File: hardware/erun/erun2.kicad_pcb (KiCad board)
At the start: 2 copper layers, 73.7 x 92.1 mm, 21 parts, among them J1 Conn_Coaxial, J10 Conn_01x03_Female, J2 HEIDENHAIN_MT25_TTL, J3 TRIGGER_TTL, J4 Conn_01x02_Female, J5 Conn_01x02_Female, J6 Conn_01x02_Female, J7 Conn_01x02_Female, J8 Conn_01x02_Female, J9 Conn_01x03_Female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

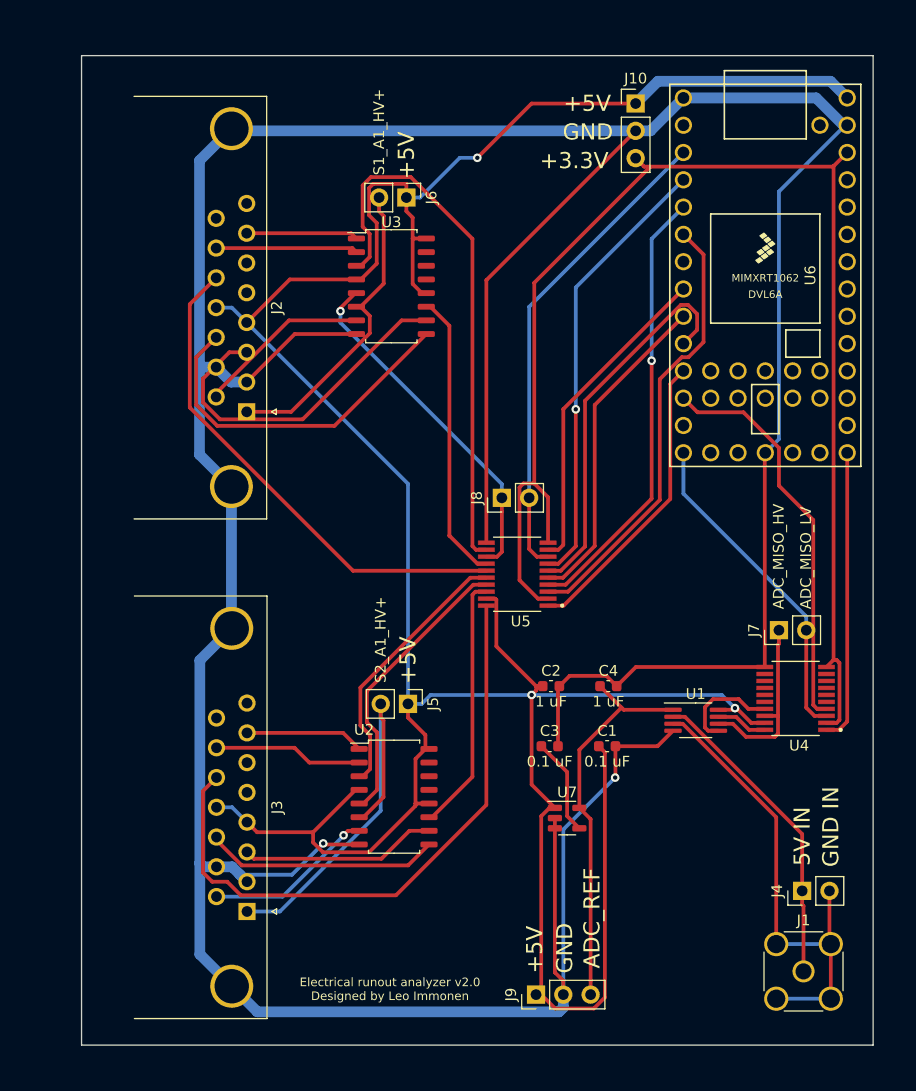
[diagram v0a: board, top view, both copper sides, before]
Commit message: Fixed clearance issues
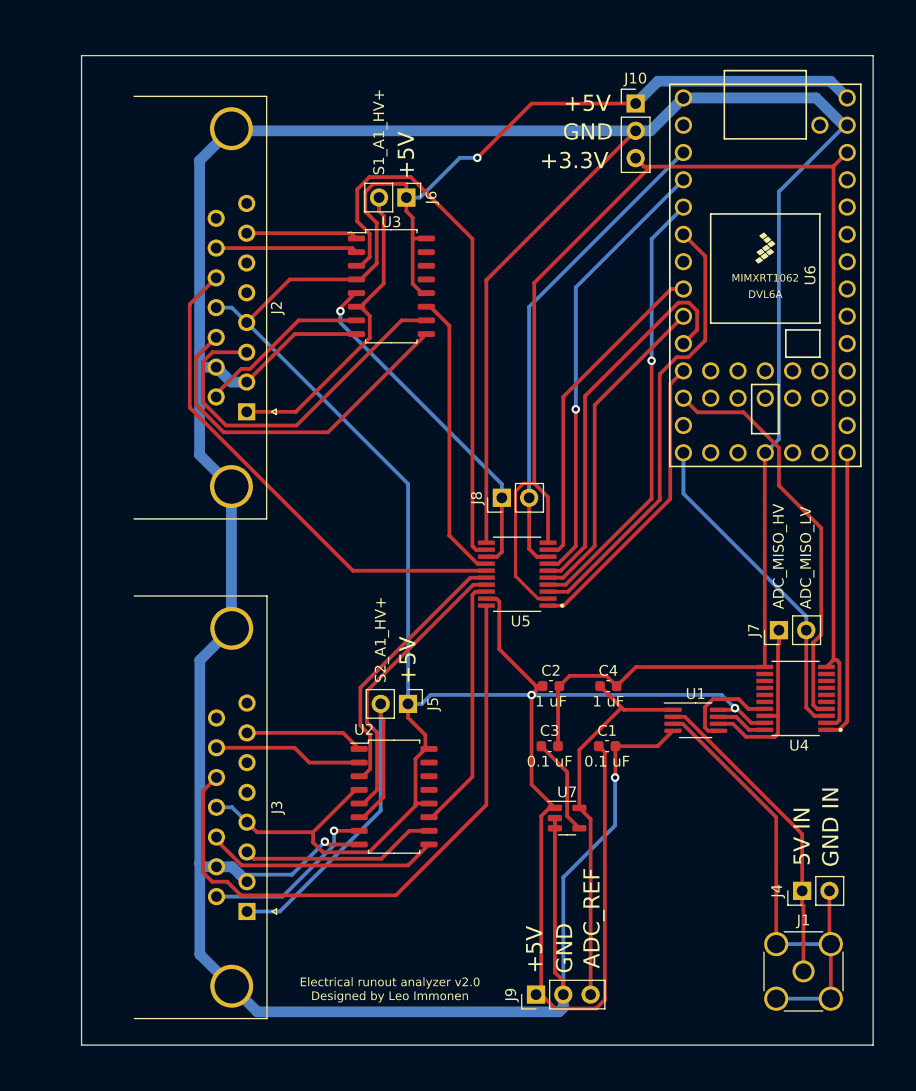
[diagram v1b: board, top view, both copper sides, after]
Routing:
- net /S1_A2_HV+: track 32.5 -> 33.9 mm
- net /S2_A1_HV-: track 15.8 -> 16.6 mm
- net /S1_A0_LV: track 30.1 -> 30.7 mm
- net /ADC_CS_LV: track 37.4 -> 38.1 mm
- net /S1_AS_LV: track 35.7 -> 36.3 mm

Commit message: Fixed some more clearance issues
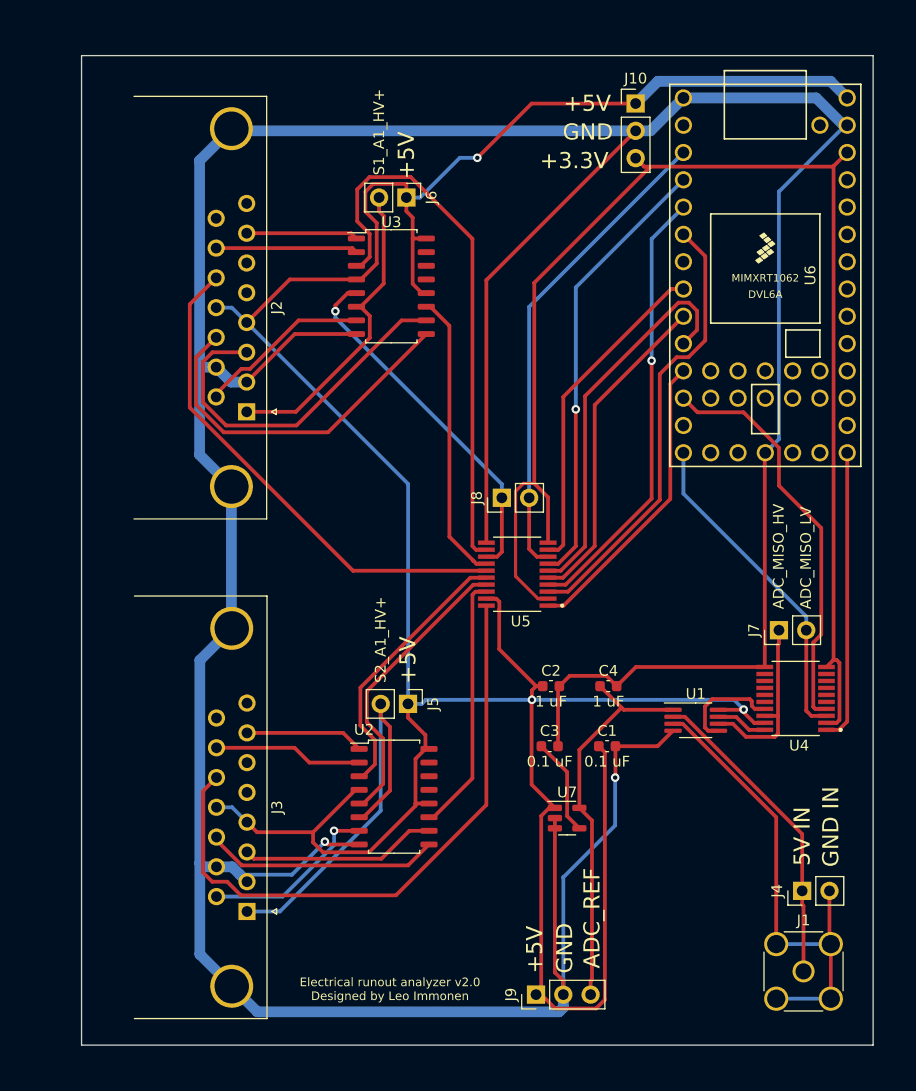
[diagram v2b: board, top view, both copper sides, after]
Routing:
- net /S1_A1_HV: track 32.6 -> 33.4 mm
- net +5V: track 279.1 -> 279.8 mm

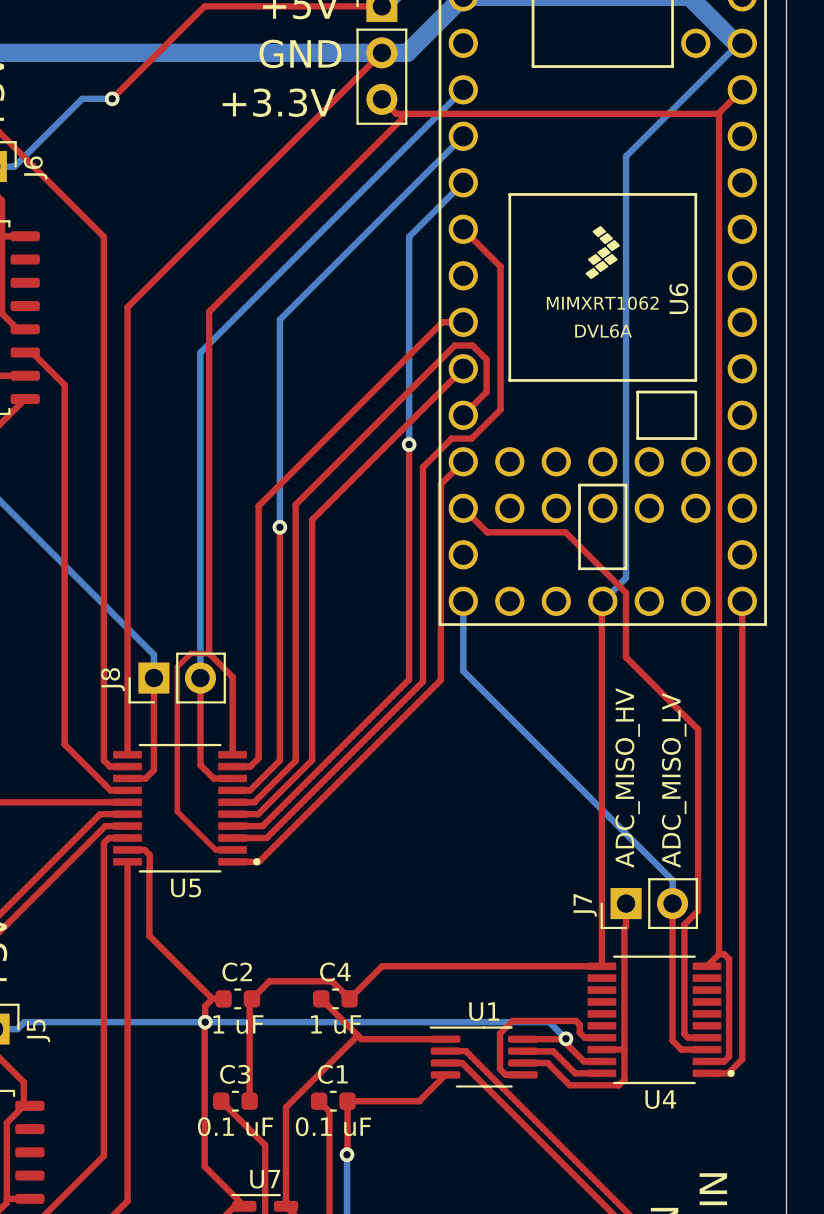
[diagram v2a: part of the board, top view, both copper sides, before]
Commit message: Added capacitors to the board
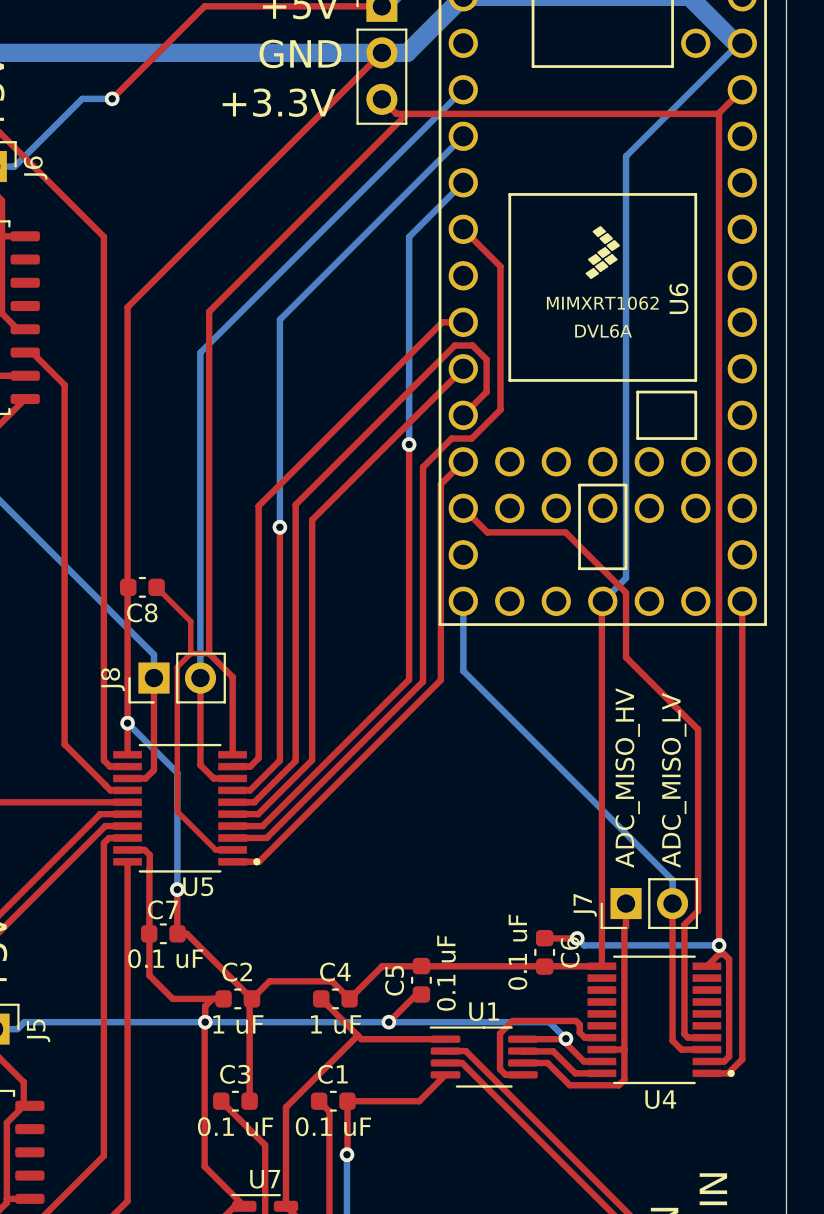
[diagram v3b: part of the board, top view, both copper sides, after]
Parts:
- added C5: 0.1 uF, Capacitor_SMD:C_0603_1608Metric, F.Cu at (63.8, 67.7)
- added C6: 0.1 uF, Capacitor_SMD:C_0603_1608Metric, F.Cu at (70.5, 66.2)
- added C7: 0.1 uF, Capacitor_SMD:C_0603_1608Metric, F.Cu at (49.7, 65.2)
- added C8: 0.1 uF, Capacitor_SMD:C_0603_1608Metric, F.Cu at (48.5, 46.2)
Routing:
- net GND: track 384.0 -> 402.2 mm, vias 2 -> 4
- net +3V3: track 128.6 -> 142.7 mm, vias 0 -> 2
- net +5V: track 279.8 -> 284.0 mm, vias 3 -> 4

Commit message: Added filled zones
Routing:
- added copper zone on B.Cu, net GND
- added copper zone on F.Cu, net GND
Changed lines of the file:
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@@
   (segment (start 74.676 97.79) (end 79.756 97.79) (width 0.35) (layer "B.Cu") (net 85))
   (segment (start 74.676 92.71) (end 79.756 92.71) (width 0.35) (layer "B.Cu") (net 85))
+  (zone (net 1) (net_name "GND") (layers F&B.Cu) (name "GND FILL") (hatch edge 0.508)
+    (connect_pads (clearance 0.508))
+    (min_thickness 0.254) (filled_areas_thickness no)
+    (fill yes (thermal_gap 0.508) (thermal_bridge_width 0.508))
+    (polygon
+      (pts
+        (xy 85.471 6.985)
+        (xy 85.725 104.394)
+        (xy 4.445 104.394)
+        (xy 4.445 6.858)
+      )
+    )
+  )
 )

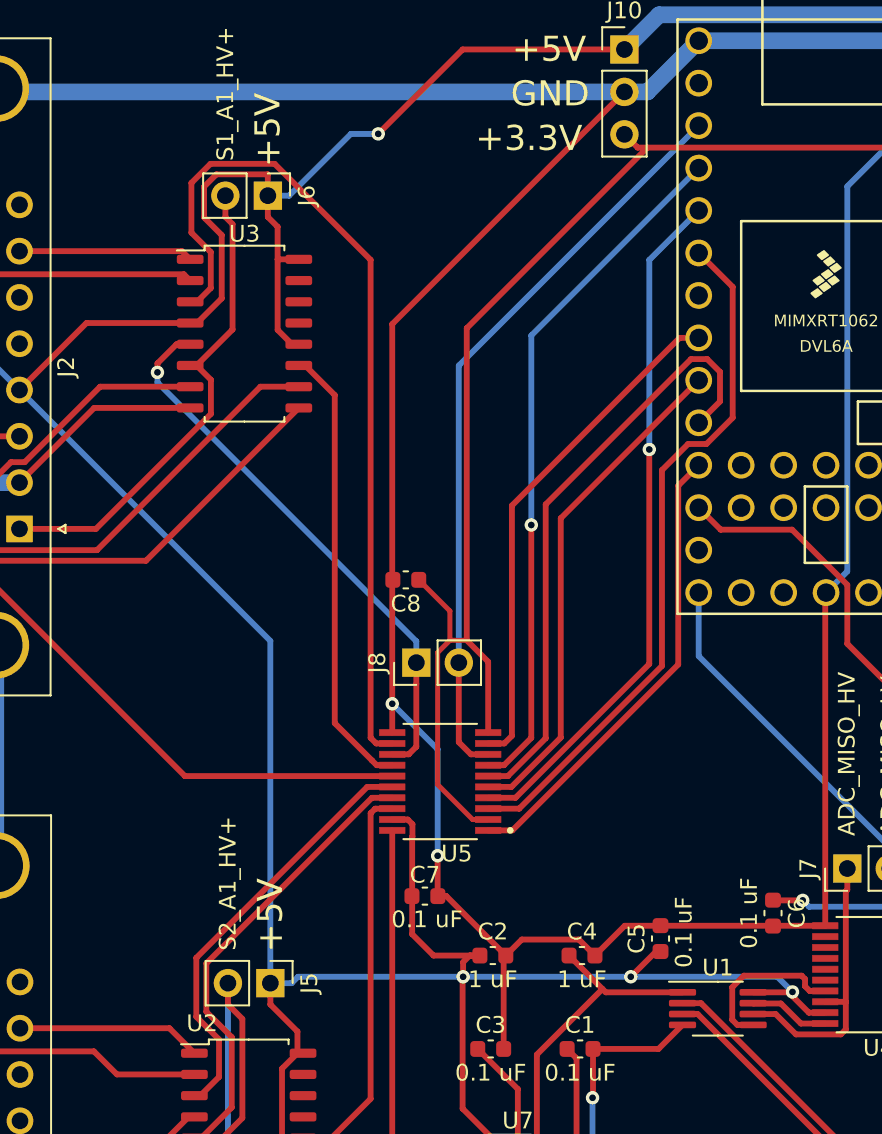
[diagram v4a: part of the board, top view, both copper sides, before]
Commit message: Added vias to filled zones
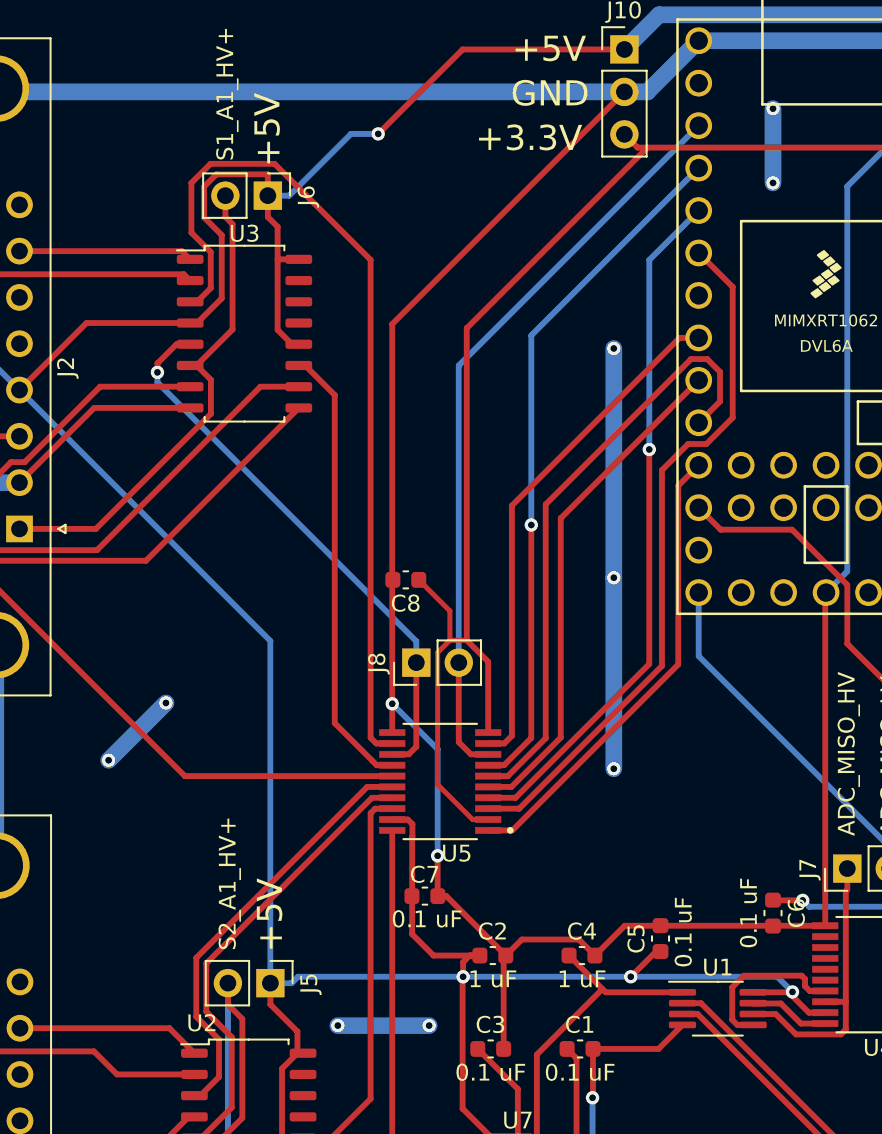
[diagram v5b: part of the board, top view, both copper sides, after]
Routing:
- net GND: track 402.2 -> 442.1 mm, vias 4 -> 13
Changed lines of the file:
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@@
   (segment (start 54.369 68.834) (end 54.496 68.707) (width 0.35) (layer "F.Cu") (net 1))
   (via (at 47.7025 53.6435) (size 0.8) (drill 0.4) (layers "F.Cu" "B.Cu") (net 1))
+  (via (at 30.734 57.023) (size 0.8) (drill 0.4) (layers "F.Cu" "B.Cu") (free) (net 1))
+  (via (at 44.45 72.898) (size 0.8) (drill 0.4) (layers "F.Cu" "B.Cu") (free) (net 1))
+  (via (at 70.485 18.034) (size 0.8) (drill 0.4) (layers "F.Cu" "B.Cu") (free) (net 1))
+  (via (at 49.911 72.898) (size 0.8) (drill 0.4) (layers "F.Cu" "B.Cu") (free) (net 1))
+  (via (at 60.96 57.531) (size 0.8) (drill 0.4) (layers "F.Cu" "B.Cu") (free) (net 1))
+  (via (at 60.96 46.101) (size 0.8) (drill 0.4) (layers "F.Cu" "B.Cu") (free) (net 1))
+  (via (at 70.485 22.479) (size 0.8) (drill 0.4) (layers "F.Cu" "B.Cu") (free) (net 1))
+  (via (at 34.163 53.594) (size 0.8) (drill 0.4) (layers "F.Cu" "B.Cu") (free) (net 1))
   (via (at 50.419 62.738) (size 0.8) (drill 0.4) (layers "F.Cu" "B.Cu") (net 1))
+  (via (at 60.96 32.385) (size 0.8) (drill 0.4) (layers "F.Cu" "B.Cu") (free) (net 1))
   (via (at 59.6877 77.2168) (size 0.8) (drill 0.4) (layers "F.Cu" "B.Cu") (net 1))
   (via (at 32.67561 83.17869) (size 0.8) (drill 0.4) (layers "F.Cu" "B.Cu") (net 1))
@@
   (segment (start 23.945 40.41) (end 22.56 39.025) (width 1) (layer "B.Cu") (net 1))
   (segment (start 54.864 98.6111) (end 54.864 97.409) (width 1) (layer "B.Cu") (net 1))
+  (segment (start 60.96 46.101) (end 60.96 57.531) (width 1) (layer "B.Cu") (net 1))
   (segment (start 81.1057 16.51) (end 74.93 22.6857) (width 0.35) (layer "B.Cu") (net 1))
   (segment (start 59.6877 81.6633) (end 59.6877 77.2168) (width 0.35) (layer "B.Cu") (net 1))
@@
   (segment (start 54.4666 99.0085) (end 54.864 98.6111) (width 1) (layer "B.Cu") (net 1))
   (segment (start 24.0103 96.63) (end 26.3888 99.0085) (width 1) (layer "B.Cu") (net 1))
+  (segment (start 49.911 72.898) (end 44.45 72.898) (width 1) (layer "B.Cu") (net 1))
+  (segment (start 60.96 32.385) (end 60.96 46.101) (width 1) (layer "B.Cu") (net 1))
   (segment (start 23.98 16.835) (end 21.0105 19.8045) (width 1) (layer "B.Cu") (net 1))
+  (segment (start 70.485 18.034) (end 70.485 22.479) (width 1) (layer "B.Cu") (net 1))
   (segment (start 22.5903 85.52) (end 21.385 85.52) (width 1) (layer "B.Cu") (net 1))
   (segment (start 24.0453 85.52) (end 24.7793 86.254) (width 1) (layer "B.Cu") (net 1))
+  (segment (start 30.734 57.023) (end 34.163 53.594) (width 1) (layer "B.Cu") (net 1))
   (segment (start 50.419 56.36) (end 50.419 62.738) (width 0.35) (layer "B.Cu") (net 1))
   (segment (start 32.67561 83.17869) (end 32.67561 83.18889) (width 0.35) (layer "B.Cu") (net 1))
